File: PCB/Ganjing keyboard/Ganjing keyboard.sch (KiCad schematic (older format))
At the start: 164 parts, among them J1 Conn_01x04, J2 AVR-ISP-6, SW1 Rotary_Encoder_Switch, U1 ATmega32A-PU, Y1 Crystal

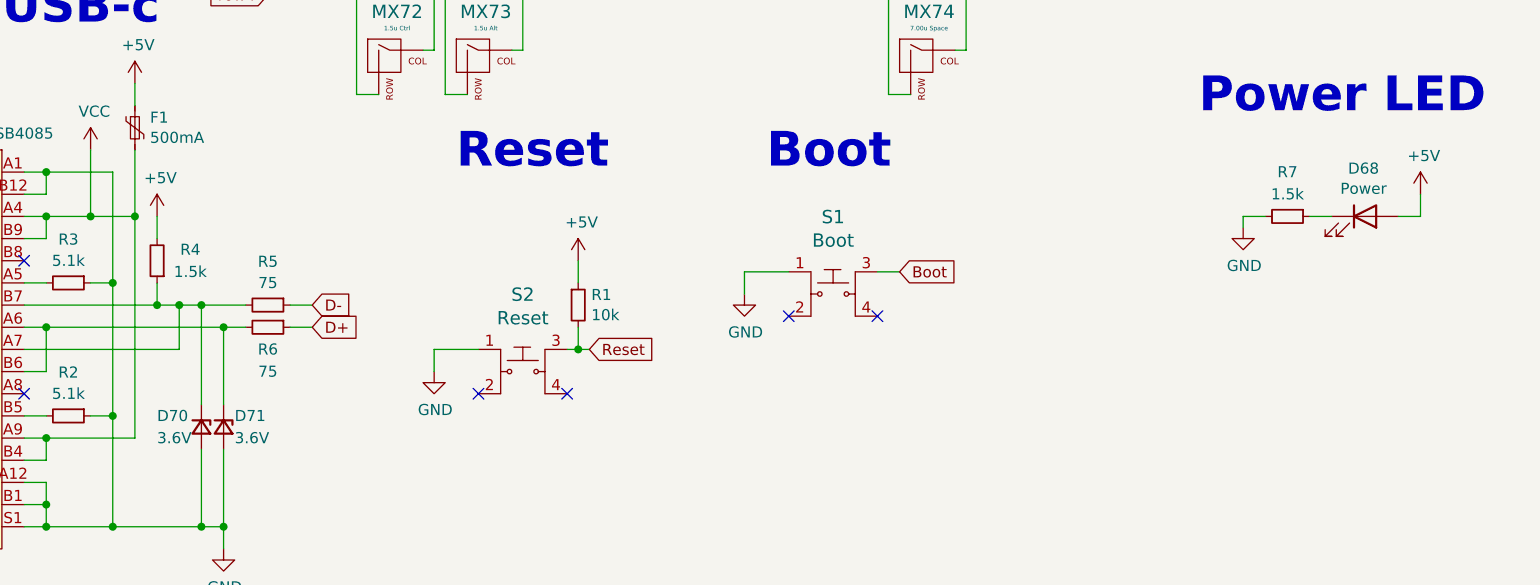
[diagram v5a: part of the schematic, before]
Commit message: cleanimg up file tree
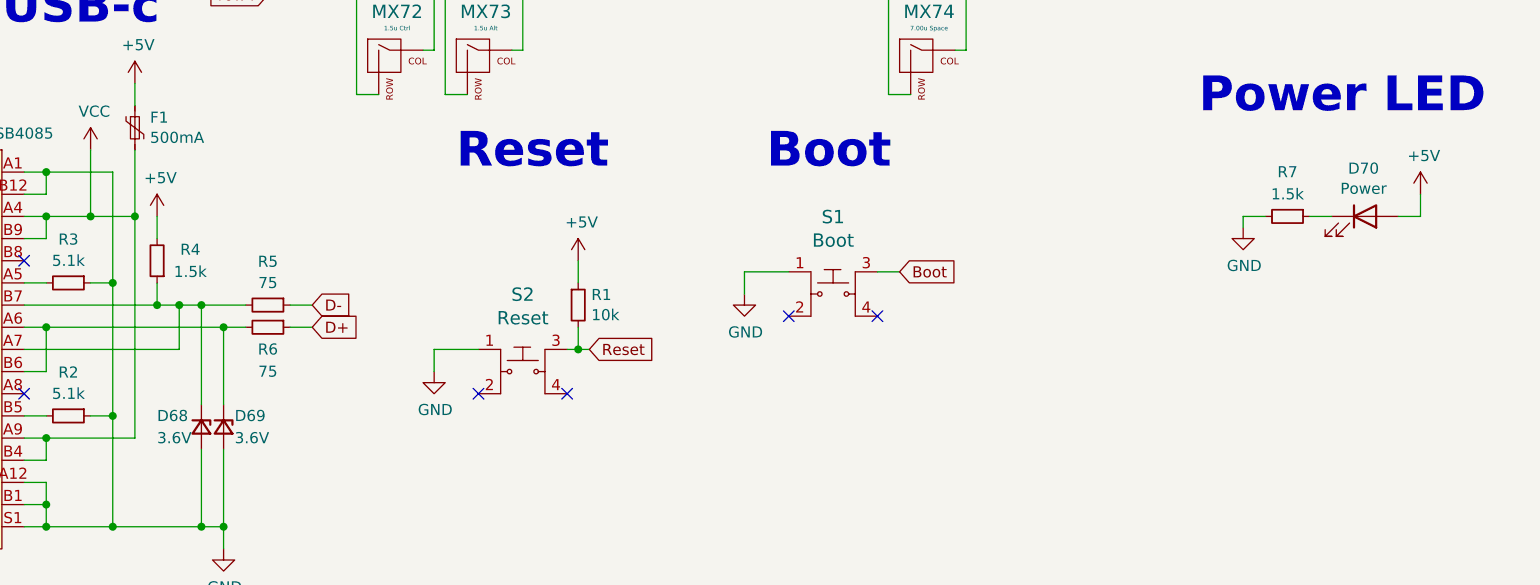
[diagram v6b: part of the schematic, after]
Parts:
- renumbered D70 to D68, D71 to D69, D68 to D70
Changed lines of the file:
@@
 $EndComp
 $Comp
-L Device:D_Zener_Small D71
+L Device:D_Zener_Small D69
 U 1 1 609A7FF8
 P 3800 6950
-F 0 "D71" V 3750 7000 50  0000 L CNN
+F 0 "D69" V 3750 7000 50  0000 L CNN
 F 1 "3.6V" V 3850 7000 50  0000 L CNN
 F 2 "Diode_THT:D_DO-35_SOD27_P5.08mm_Vertical_AnodeUp" V 3800 6950 50  0001 C CNN
@@
 Connection ~ 3300 7400
 $Comp
-L Device:D_Zener_Small D70
+L Device:D_Zener_Small D68
 U 1 1 5F4FECAA
 P 3700 6950
-F 0 "D70" V 3650 6750 50  0000 L CNN
+F 0 "D68" V 3650 6750 50  0000 L CNN
 F 1 "3.6V" V 3750 6750 50  0000 L CNN
 F 2 "Diode_THT:D_DO-35_SOD27_P5.08mm_Vertical_AnodeUp" V 3700 6950 50  0001 C CNN
@@
 	9200 5900 9200 6000
 $Comp
-L Device:LED D68
+L Device:LED D70
 U 1 1 5F4D0275
 P 8950 6000
-F 0 "D68" H 8943 6216 50  0000 C CNN
+F 0 "D70" H 8943 6216 50  0000 C CNN
 F 1 "Power" H 8943 6125 50  0000 C CNN
 F 2 "Keyboard:LED_D3.0mm" H 8950 6000 50  0001 C CNN

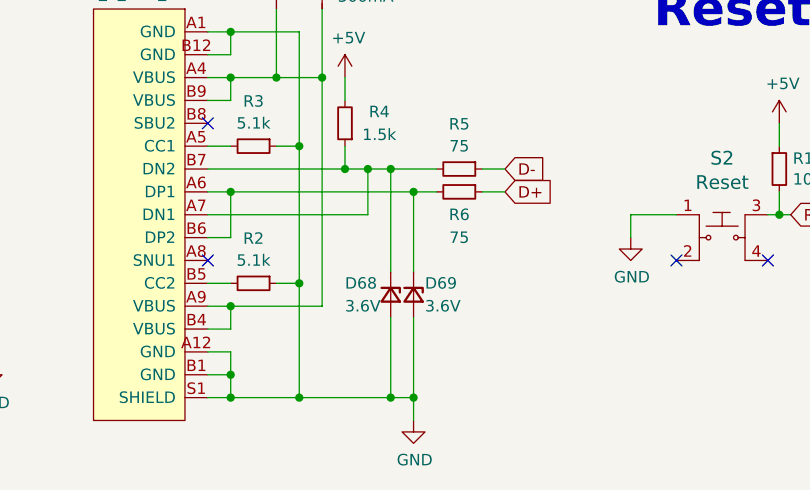
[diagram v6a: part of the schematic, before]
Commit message: switching diode names
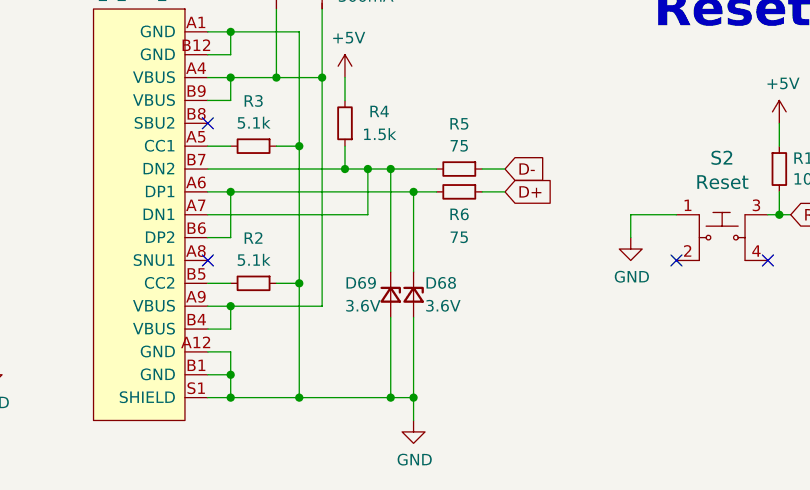
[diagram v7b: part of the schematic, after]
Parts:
- renumbered D69 to D68, D68 to D69
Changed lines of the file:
@@
 $EndComp
 $Comp
-L Device:D_Zener_Small D69
+L Device:D_Zener_Small D68
 U 1 1 609A7FF8
 P 3800 6950
-F 0 "D69" V 3750 7000 50  0000 L CNN
+F 0 "D68" V 3750 7000 50  0000 L CNN
 F 1 "3.6V" V 3850 7000 50  0000 L CNN
 F 2 "Diode_THT:D_DO-35_SOD27_P5.08mm_Vertical_AnodeUp" V 3800 6950 50  0001 C CNN
@@
 Connection ~ 3300 7400
 $Comp
-L Device:D_Zener_Small D68
+L Device:D_Zener_Small D69
 U 1 1 5F4FECAA
 P 3700 6950
-F 0 "D68" V 3650 6750 50  0000 L CNN
+F 0 "D69" V 3650 6750 50  0000 L CNN
 F 1 "3.6V" V 3750 6750 50  0000 L CNN
 F 2 "Diode_THT:D_DO-35_SOD27_P5.08mm_Vertical_AnodeUp" V 3700 6950 50  0001 C CNN

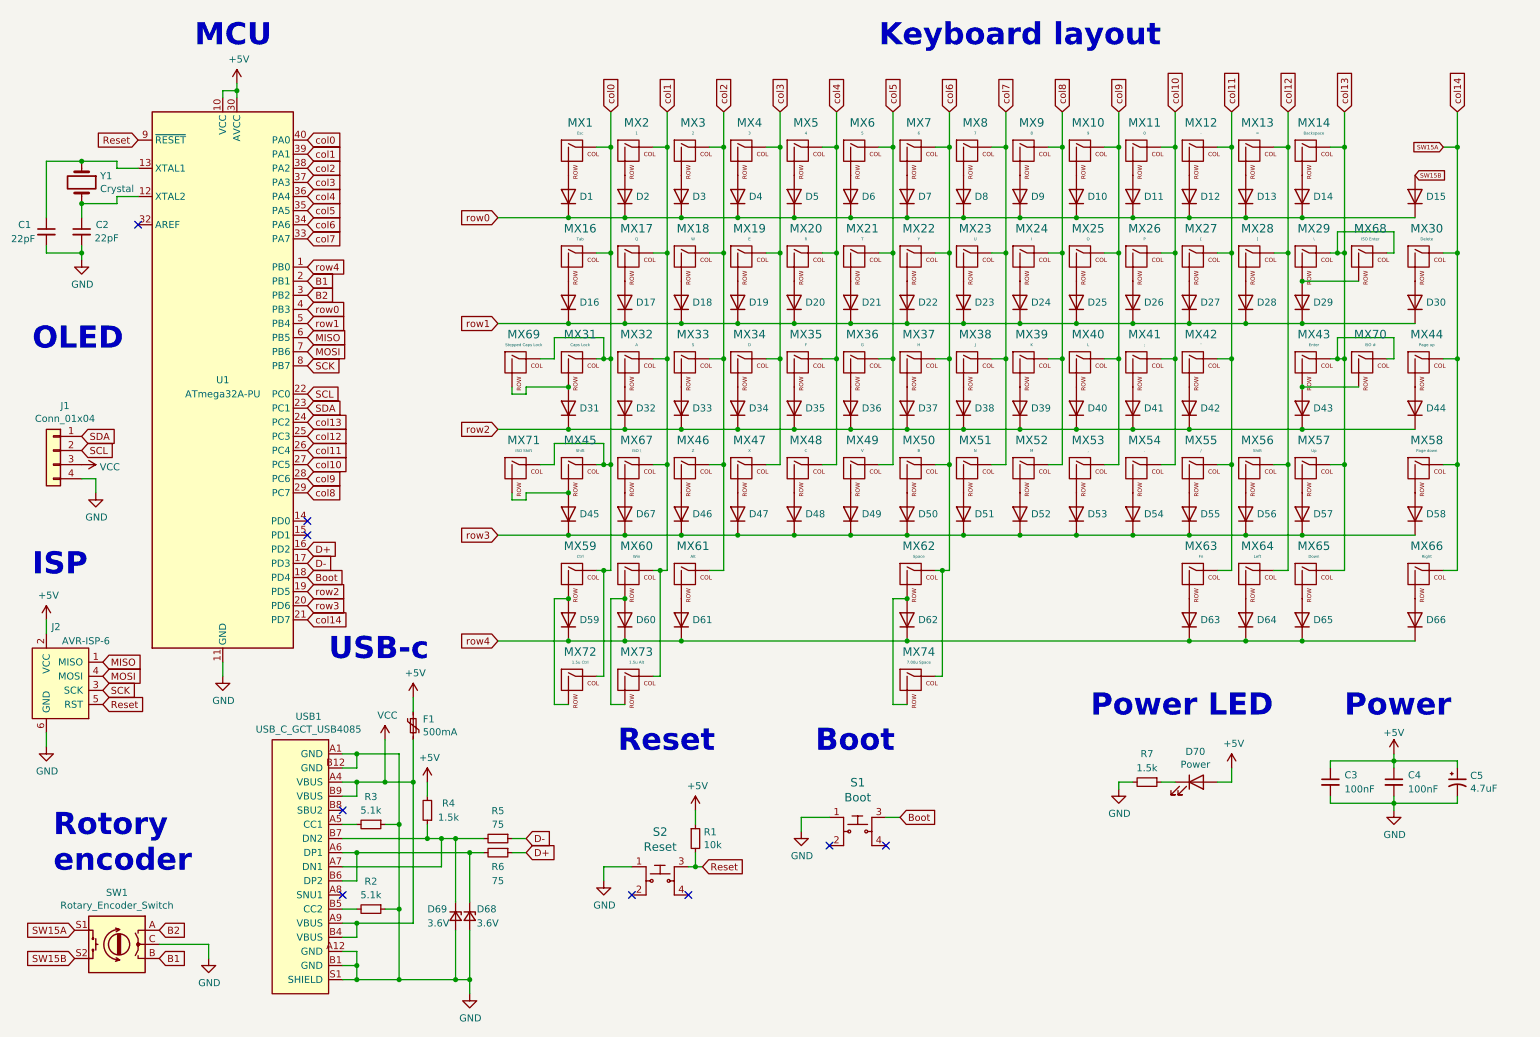
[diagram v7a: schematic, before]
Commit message: Reordering references
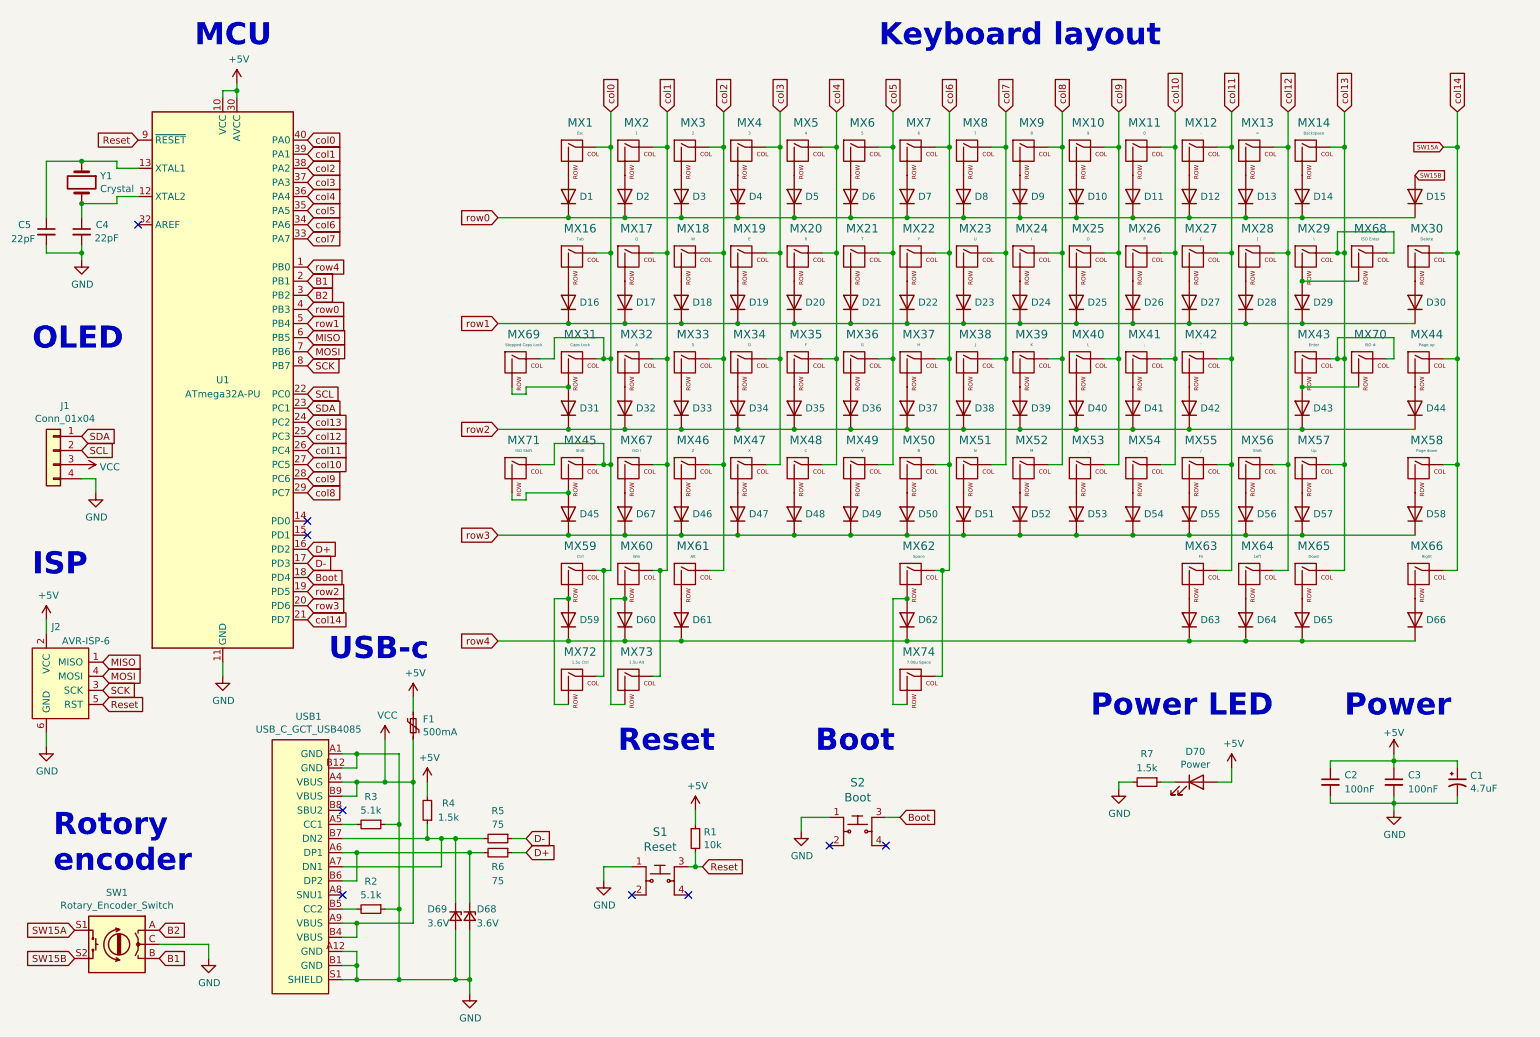
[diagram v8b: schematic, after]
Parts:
- renumbered C5 to C1, C3 to C2, C4 to C3, C2 to C4, C1 to C5, S2 to S1, S1 to S2
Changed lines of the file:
@@
 NoConn ~ 6750 6450
 $Comp
-L Device:C_Small C4
+L Device:C_Small C3
 U 1 1 609AA0F0
 P 10350 6000
-F 0 "C4" H 10450 6050 50  0000 L CNN
+F 0 "C3" H 10450 6050 50  0000 L CNN
 F 1 "100nF" H 10450 5950 50  0000 L CNN
 F 2 "Keyboard:C_Disc_D4.3mm_W1.9mm_P5.00mm" H 10350 6000 50  0001 C CNN
@@
 $EndComp
 $Comp
-L Device:C_Small C1
+L Device:C_Small C5
 U 1 1 609A5F14
 P 800 2100
-F 0 "C1" H 600 2150 50  0000 L CNN
+F 0 "C5" H 600 2150 50  0000 L CNN
 F 1 "22pF" H 550 2050 50  0000 L CNN
 F 2 "Keyboard:C_Disc_D3.0mm_W1.6mm_P2.50mm" H 800 2100 50  0001 C CNN
@@
 	1050 1900 1300 1900
 $Comp
-L Device:C_Small C2
+L Device:C_Small C4
 U 1 1 5F4C5281
 P 1050 2100
-F 0 "C2" H 1150 2150 50  0000 L CNN
+F 0 "C4" H 1150 2150 50  0000 L CNN
 F 1 "22pF" H 1142 2055 50  0000 L CNN
 F 2 "Keyboard:C_Disc_D3.0mm_W1.6mm_P2.50mm" H 1050 2100 50  0001 C CNN
@@
 Boot
 $Comp
-L Ganjing-keyboard-rescue:1825910-7-dk_Tactile-Switches S1
+L Ganjing-keyboard-rescue:1825910-7-dk_Tactile-Switches S2
 U 1 1 5F4E706C
 P 6550 6350
-F 0 "S1" H 6550 6697 60  0000 C CNN
+F 0 "S2" H 6550 6697 60  0000 C CNN
 F 1 "Boot" H 6550 6591 60  0000 C CNN
 F 2 "digikey-footprints:Switch_Tactile_THT_6x6mm" H 6750 6550 60  0001 L CNN
@@
 	4750 6600 4750 6700
 $Comp
-L Ganjing-keyboard-rescue:1825910-7-dk_Tactile-Switches S2
+L Ganjing-keyboard-rescue:1825910-7-dk_Tactile-Switches S1
 U 1 1 5F4DDD6B
 P 5150 6700
-F 0 "S2" H 5150 7047 60  0000 C CNN
+F 0 "S1" H 5150 7047 60  0000 C CNN
 F 1 "Reset" H 5150 6941 60  0000 C CNN
 F 2 "digikey-footprints:Switch_Tactile_THT_6x6mm" H 5350 6900 60  0001 L CNN
@@
 	9900 6100 9900 6150
 $Comp
-L Device:CP1_Small C5
+L Device:CP1_Small C1
 U 1 1 5F4C9663
 P 10800 6000
-F 0 "C5" H 10891 6046 50  0000 L CNN
+F 0 "C1" H 10891 6046 50  0000 L CNN
 F 1 "4.7uF" H 10891 5955 50  0000 L CNN
 F 2 "Keyboard:CP_Radial_D4.0mm_P1.50mm" H 10800 6000 50  0001 C CNN
@@
 $EndComp
 $Comp
-L Device:C_Small C3
+L Device:C_Small C2
 U 1 1 5F4C8C59
 P 9900 6000
-F 0 "C3" H 10000 6050 50  0000 L CNN
+F 0 "C2" H 10000 6050 50  0000 L CNN
 F 1 "100nF" H 10000 5950 50  0000 L CNN
 F 2 "Keyboard:C_Disc_D4.3mm_W1.9mm_P5.00mm" H 9900 6000 50  0001 C CNN
